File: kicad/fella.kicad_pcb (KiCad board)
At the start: 2 copper layers, 284.9 x 96.5 mm, 115 parts, among them J1 Conn_02x06_Odd_Even, J2 DE15_Receptacle_HighDensity_M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, J3 USB_C_Receptacle_USB2.0_14P, J4 DE9_Plug_MountingHoles, J5 DB25_Receptacle_MountingHoles, J6 Conn_02x18_Top_Bottom, J7 Conn_01x02, Q1 BC547, Q2 BC547, SW2 Reset, U10 74HC00, U11 6264, U12 6264, U13 74HC32, U17 74HC174, U18 XC9536PC44, U19 74HC244, U2 NE555P, U20 74HC574, U21 74HC245, U22 74HC02, U24 6264, U25 74HC574, U26 2764, U27 74HC166, U28 74HC244, U29 6522, U3 74HC138, U30 6551, U31 6551, U32 MAX232, U33 CH340N, U34 24LC256, U35 74HC244, U36 74HC244, U37 74HC245, U38 74HC574, U4 6502, U5 74HC08, U7 74HC138, U8 6264, U9 27256, X1 ACO-25.175MHz-A, X2 ACO-1.8432MHz-A

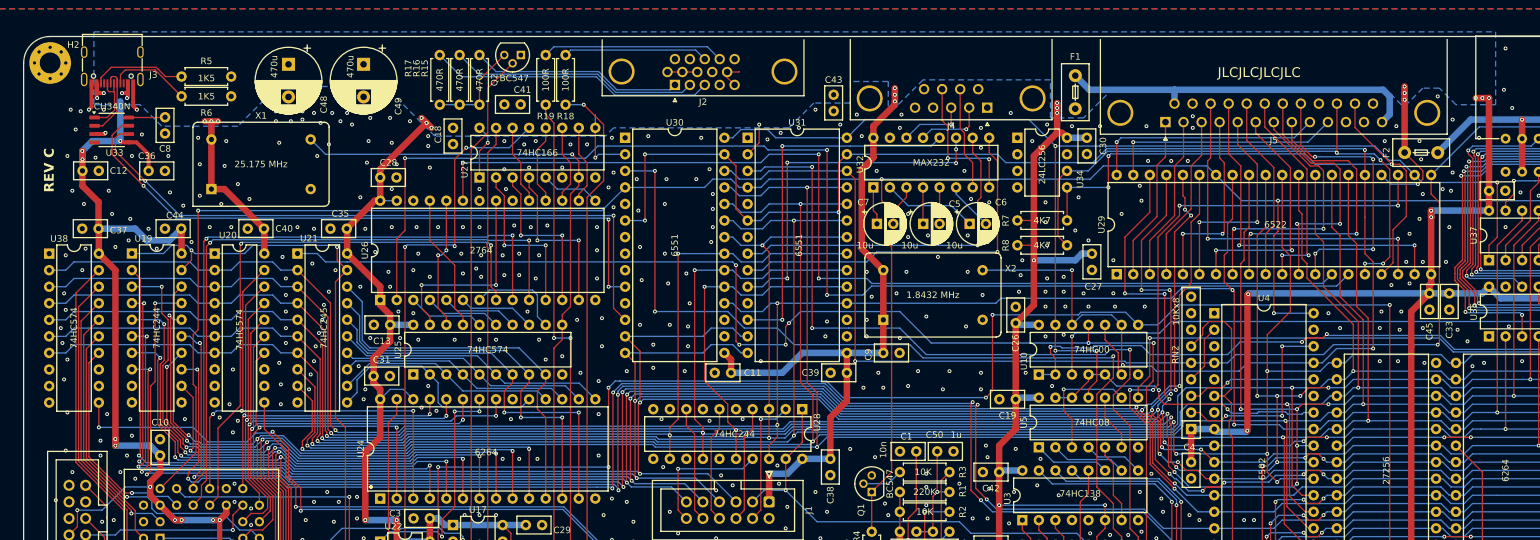
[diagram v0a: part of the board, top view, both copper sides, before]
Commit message: hw: rev D - replace DB25 connector footprint with available one
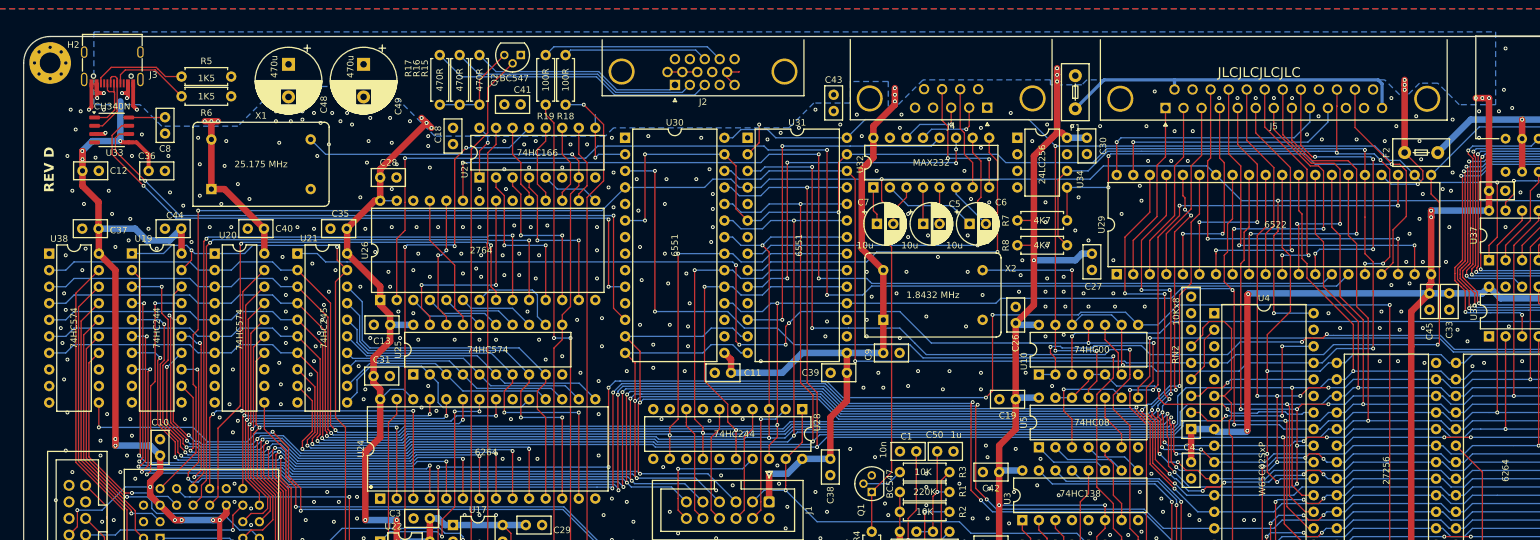
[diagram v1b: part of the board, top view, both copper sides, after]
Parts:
- J5: footprint Connector_Dsub:DSUB-25_Female_Horizontal_P2.77x2.84mm_EdgePinOffset9.90mm_Housed_MountingHolesOffset11.32mm -> Connector_Dsub:DSUB-25_Socket_Horizontal_P2.77x2.84mm_EdgePinOffset7.70mm_Housed_MountingHolesOffset9.12mm
- U4: value 6502 -> W65C02SxP
- moved F1 5.08 mm to (233.7, 97.1), turned to 90 degrees
- moved J5 2.17 mm to (247.5, 97.0)
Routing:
- net VCC: track 1010.3 -> 1016.7 mm
- net Net-(J5-P23): track 91.3 -> 93.5 mm
- net Net-(U29-PA7): track 47.0 -> 49.2 mm
- net Net-(U29-PA6): track 41.1 -> 43.2 mm
- net Net-(U29-PA4): track 33.5 -> 35.7 mm
- net Net-(U29-PA3): track 29.9 -> 32.0 mm
- net Net-(U29-PA2): track 25.6 -> 27.8 mm
- net Net-(U29-PA1): track 25.5 -> 27.7 mm
- net Net-(U29-PA0): track 25.4 -> 27.6 mm
- net Net-(U29-CA2): track 36.2 -> 38.4 mm
- net Net-(U29-CA1): track 36.0 -> 38.1 mm
- net Net-(J5-P24): track 92.2 -> 94.4 mm
- net Net-(J5-P21): track 44.6 -> 46.7 mm
- net Net-(J5-P20): track 38.6 -> 40.8 mm
- net Net-(J5-P19): track 33.1 -> 35.2 mm
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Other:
- board text added: "REV D"
- board text removed: "REV C"
